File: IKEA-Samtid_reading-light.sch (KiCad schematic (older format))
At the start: 29 parts, among them IC1 ATTINY25-S, P1 CONN_2, U1 MCP1804-SOT23-5, U2 PT4115-SOT89-5

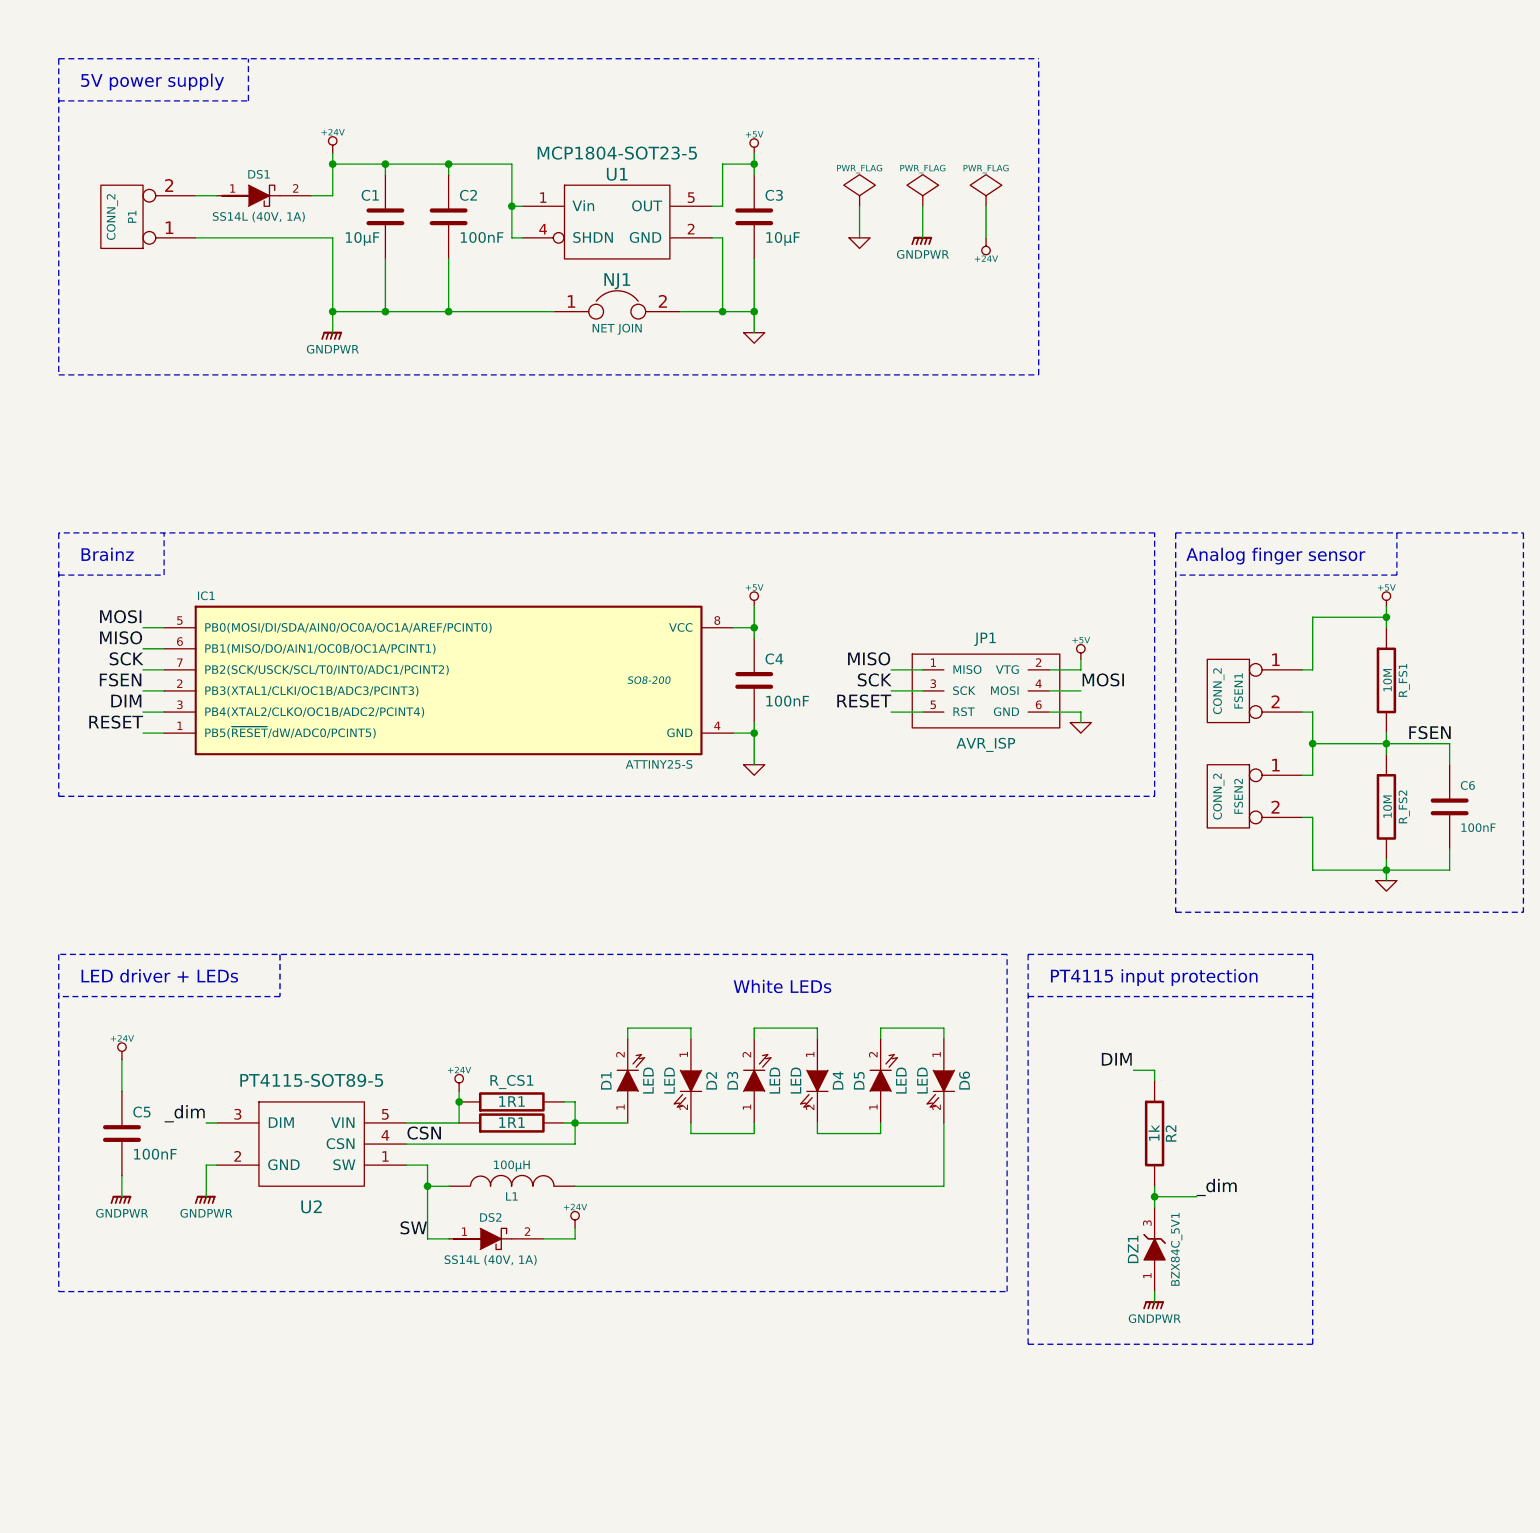
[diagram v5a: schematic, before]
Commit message: Tweaks.
1) C6: 100nF --> 22nF (faster response to finger touch). RC < 100ms.
2) Added 10k pull-down for _dim on PT4115 to prevent / reduce LED flash on power-up.
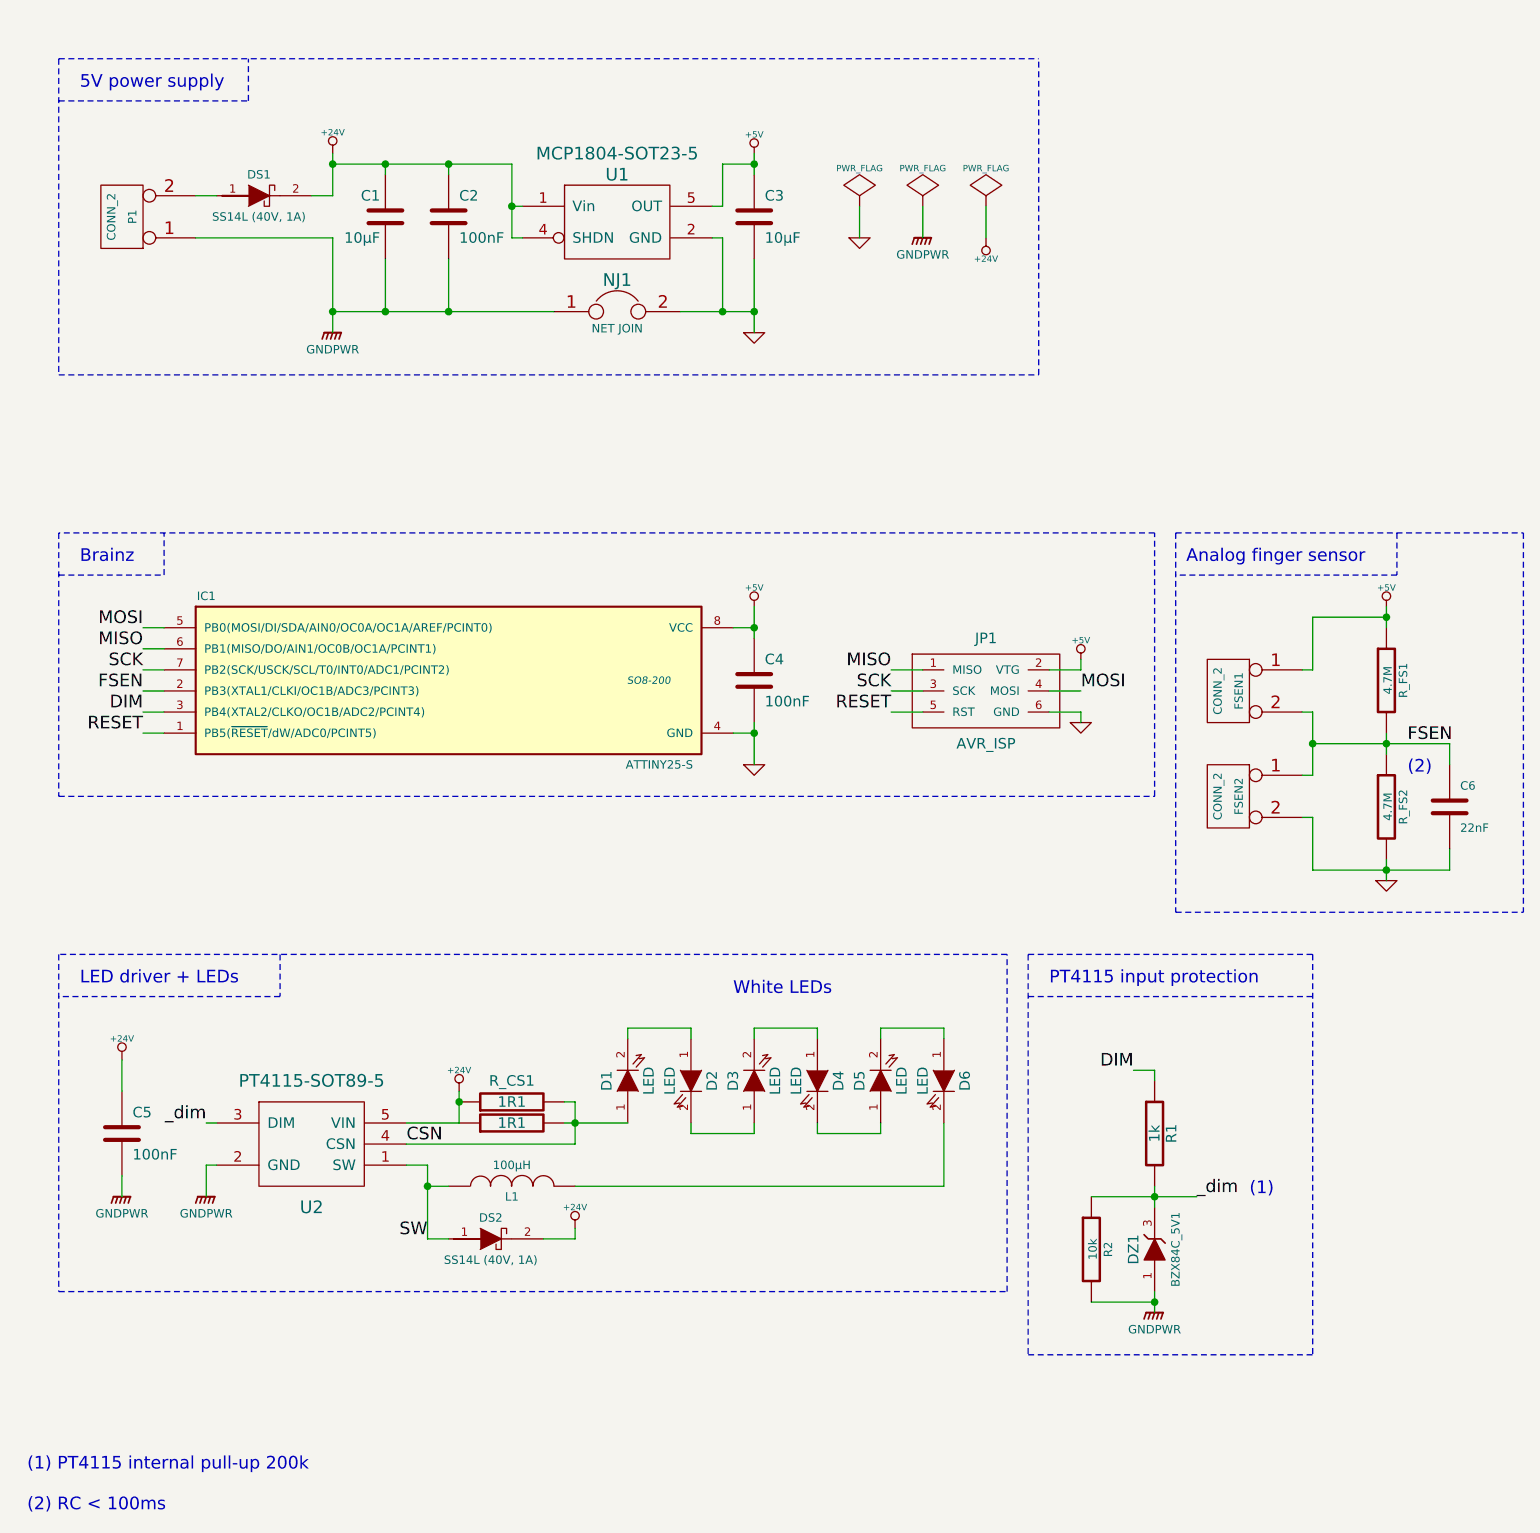
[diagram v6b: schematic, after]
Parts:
- added R2: 10k, symbol R
- C6: value 100nF -> 22nF
- R_FS1, R_FS2: value 10M -> 4.7M
- renumbered R2 to R1
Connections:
- net GNDPWR: now also R2.2
- net _dim: now also R2.1
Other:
- note added: "(1)"
- note added: "(1) PT4115 internal pull-up 200k\n\n(2) RC < 100ms"
- note added: "(2)"
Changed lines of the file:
@@
 Sheet 1 1
 Title "IKEA-Samtid_reading-light"
-Date "29 May 2014"
-Rev "0.10"
+Date "22 Jun 2014"
+Rev "0.11"
 Comp "2014 - blog.spitzenpfeil.org"
 Comment1 ""
@@
 $EndComp
 Wire Wire Line
-	5950 6150 6150 6150
+	5650 6150 6150 6150
 Wire Wire Line
 	5850 5550 5950 5550
@@
 	5150 1450 5150 1600
 Wire Wire Line
-	5950 6600 5950 6650
+	5950 6600 5950 6700
 Wire Wire Line
 	5950 6100 5950 6200
@@
 _dim
 $Comp
-L R R2
+L R R1
 U 1 1 509FF5DB
 P 5950 5850
-F 0 "R2" V 6030 5850 50  0000 C CNN
+F 0 "R1" V 6030 5850 50  0000 C CNN
 F 1 "1k" V 5950 5850 50  0000 C CNN
 F 2 "" H 5950 5850 60  0001 C CNN
@@
 P 7050 3700
 F 0 "R_FS1" V 7130 3700 40  0000 C CNN
-F 1 "10M" V 7057 3701 40  0000 C CNN
+F 1 "4.7M" V 7057 3701 40  0000 C CNN
 F 2 "" V 6980 3700 30  0000 C CNN
 F 3 "" H 7050 3700 30  0000 C CNN
@@
 P 7050 4300
 F 0 "R_FS2" V 7130 4300 40  0000 C CNN
-F 1 "10M" V 7057 4301 40  0000 C CNN
+F 1 "4.7M" V 7057 4301 40  0000 C CNN
 F 2 "" V 6980 4300 30  0000 C CNN
 F 3 "" H 7050 4300 30  0000 C CNN
@@
 PT4115 input protection
 Wire Notes Line
-	5350 6850 6700 6850
+	5350 6900 6700 6900
 Wire Notes Line
 	5350 5200 6700 5200
@@
 	5350 5000 6700 5000
 Wire Notes Line
-	6700 5000 6700 6850
-Wire Notes Line
-	5350 6850 5350 5000
+	6700 5000 6700 6900
+Wire Notes Line
+	5350 5000 5350 6900
 Text Notes 850  3150 0    60   ~ 0
 Brainz
@@
 L GNDPWR #PWR017
 U 1 1 53852D77
-P 5950 6650
-F 0 "#PWR017" H 5950 6700 40  0001 C CNN
-F 1 "GNDPWR" H 5950 6570 40  0000 C CNN
-F 2 "" H 5950 6650 60  0000 C CNN
-F 3 "" H 5950 6650 60  0000 C CNN
-	1    5950 6650
+P 5950 6700
+F 0 "#PWR017" H 5950 6750 40  0001 C CNN
+F 1 "GNDPWR" H 5950 6620 40  0000 C CNN
+F 2 "" H 5950 6700 60  0000 C CNN
+F 3 "" H 5950 6700 60  0000 C CNN
+	1    5950 6700
 	1    0    0    -1
 $EndComp
@@
 P 7350 4300
 F 0 "C6" H 7400 4400 40  0000 L CNN
-F 1 "100nF" H 7400 4200 40  0000 L CNN
+F 1 "22nF" H 7400 4200 40  0000 L CNN
 F 2 "" H 7388 4150 30  0000 C CNN
 F 3 "" H 7350 4300 60  0000 C CNN
@@
 Wire Notes Line
 	7700 3000 7700 4800
+$Comp
+L R R2
+U 1 1 53A60C03
+P 5650 6400
+F 0 "R2" V 5730 6400 40  0000 C CNN
+F 1 "10k" V 5657 6401 40  0000 C CNN
+F 2 "" V 5580 6400 30  0000 C CNN
+F 3 "" H 5650 6400 30  0000 C CNN
+	1    5650 6400
+	1    0    0    -1
+$EndComp
+Wire Wire Line
+	5650 6650 5950 6650
+Connection ~ 5950 6650
+Text Notes 600  7650 0    60   ~ 0
+(1) PT4115 internal pull-up 200k\n\n(2) RC < 100ms
+Text Notes 6400 6150 0    60   ~ 0
+(1)
+Text Notes 7150 4150 0    60   ~ 0
+(2)
 $EndSCHEMATC

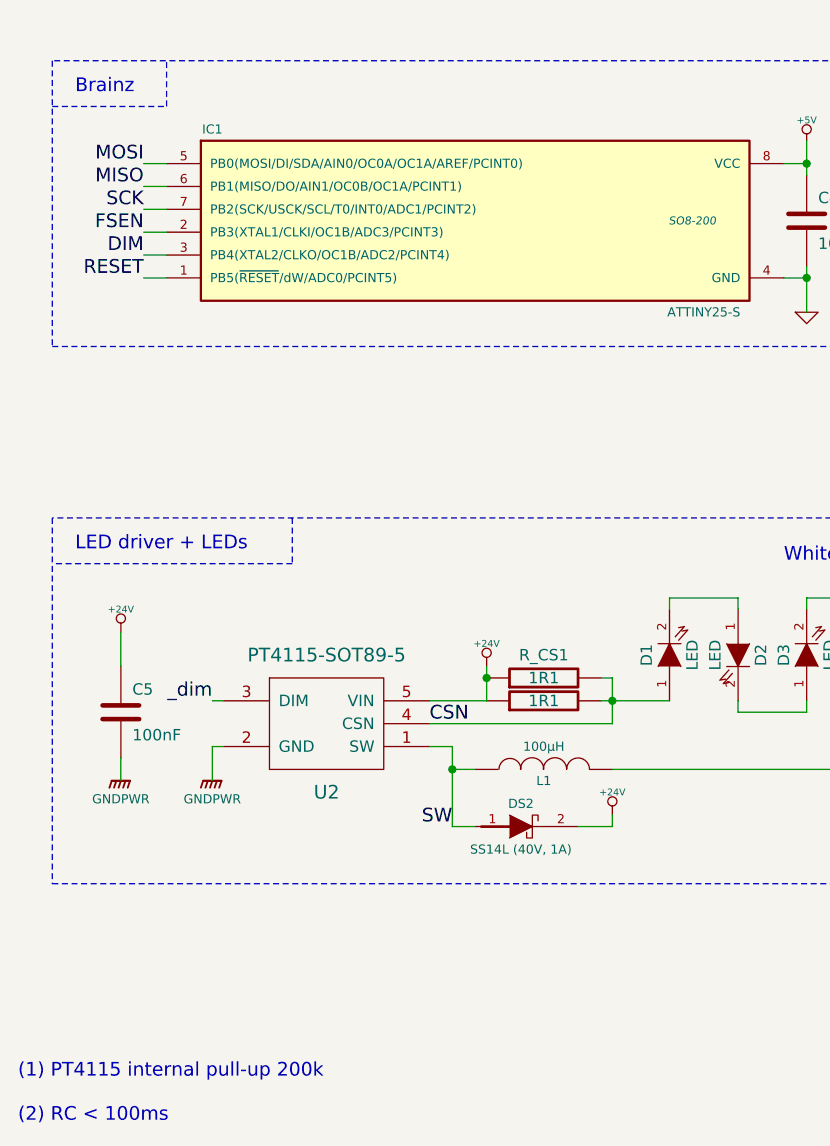
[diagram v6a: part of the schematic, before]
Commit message: Added comment to schematic (ATtiny13 vs. ATtiny25/45/85).
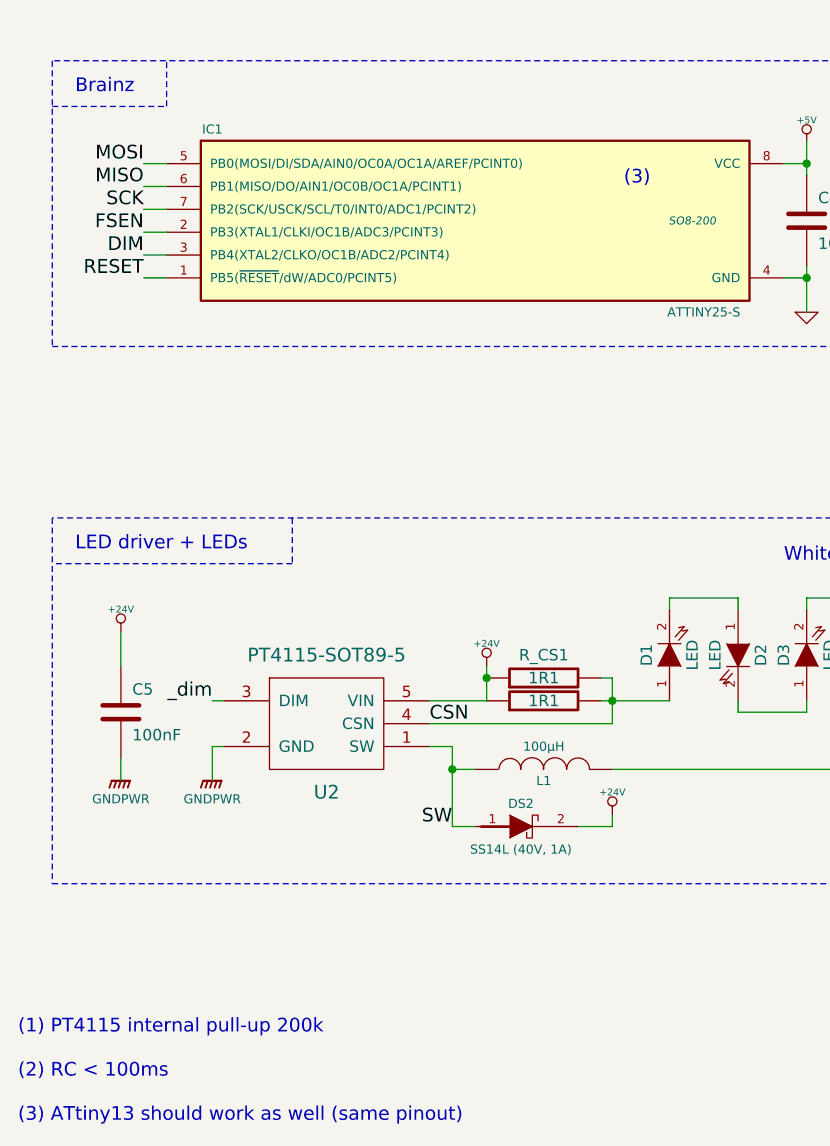
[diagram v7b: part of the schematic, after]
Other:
- note added: "(1) PT4115 internal pull-up 200k\n\n(2) RC < 100ms\n\n(3) ATtiny13 should work as well (same pinout)"
- note added: "(3)"
- note removed: "(1) PT4115 internal pull-up 200k\n\n(2) RC < 100ms"
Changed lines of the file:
@@
 Connection ~ 5950 6650
 Text Notes 600  7650 0    60   ~ 0
-(1) PT4115 internal pull-up 200k\n\n(2) RC < 100ms
+(1) PT4115 internal pull-up 200k\n\n(2) RC < 100ms\n\n(3) ATtiny13 should work as well (same pinout)
 Text Notes 6400 6150 0    60   ~ 0
 (1)
 Text Notes 7150 4150 0    60   ~ 0
 (2)
+Text Notes 3250 3550 0    60   ~ 0
+(3)
 $EndSCHEMATC
